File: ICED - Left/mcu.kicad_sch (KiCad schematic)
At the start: 48 parts, among them P1 Conn_ARM_JTAG_SWD_10, P2 DX07S024XJ1R1100, P3 CONN_17, P4 692121130100, P5 RGB Out, Q1 TC1264, U1 MK20DX256VLH7, X1 NX3225SA-16.000MHZ-STD-CSR-

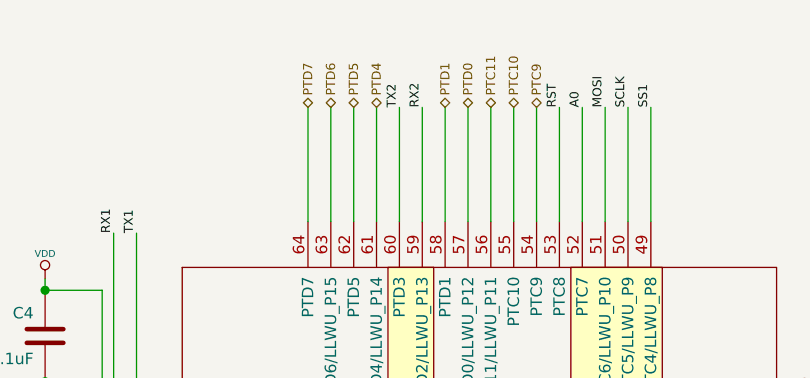
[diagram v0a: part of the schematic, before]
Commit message: mostly routed
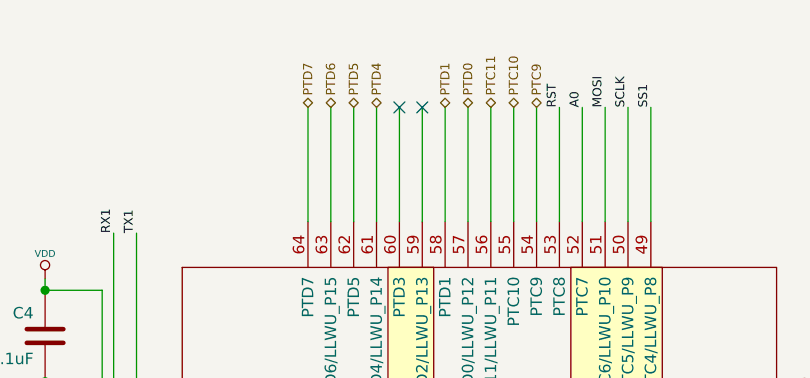
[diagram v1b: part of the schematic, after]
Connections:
- net RX2: no longer U1.59 (PTD2/LLWU_P13)
- net TX2: no longer U1.60 (PTD3)
- no-connect marks 16 -> 18
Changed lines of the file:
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@@
   (no_connect (at 134.62 111.76))
   (no_connect (at 137.16 111.76))
+  (no_connect (at 139.7 22.86))
+  (no_connect (at 142.24 22.86))
   (no_connect (at 228.6 85.09))
   (wire (pts (xy 16.51 63.5) (xy 16.51 64.77))
@@
     (effects (font (size 0.9906 0.9906)) (justify left bottom))
   )
-  (label "TX2" (at 139.7 22.86 90)
-    (effects (font (size 0.9906 0.9906)) (justify left bottom))
-  )
   (label "SWD_CLK" (at 139.7 146.05 270)
     (effects (font (size 0.9906 0.9906)) (justify right bottom))
   )
-  (label "RX2" (at 142.24 22.86 90)
-    (effects (font (size 0.9906 0.9906)) (justify left bottom))
-  )
   (label "RX0" (at 144.78 124.46 270)

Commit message: Second Revision Finalised
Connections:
- net INTB: no longer P3.14, P3.15, R3.1, R5.1, U1.35 (PTB0/LLWU_P5), U1.36 (PTB1)
- new net SCL0: P3.15, R3.1, U1.35 (PTB0/LLWU_P5)
- new net SDA0: P3.14, R5.1, U1.36 (PTB1)
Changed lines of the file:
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@@
   (junction (at 238.76 85.09) (diameter 1.016) (color 0 0 0 0))
   (junction (at 240.03 135.89) (diameter 1.016) (color 0 0 0 0))
-  (junction (at 240.03 148.59) (diameter 1.016) (color 0 0 0 0))
   (junction (at 240.03 153.67) (diameter 1.016) (color 0 0 0 0))
   (junction (at 242.57 46.99) (diameter 1.016) (color 0 0 0 0))
   (junction (at 245.11 135.89) (diameter 1.016) (color 0 0 0 0))
-  (junction (at 245.11 148.59) (diameter 1.016) (color 0 0 0 0))
   (junction (at 245.11 151.13) (diameter 1.016) (color 0 0 0 0))
   (junction (at 245.11 156.21) (diameter 1.016) (color 0 0 0 0))
@@
     (stroke (width 0) (type solid) (color 0 0 0 0))
   )
-  (wire (pts (xy 233.68 148.59) (xy 240.03 148.59))
+  (wire (pts (xy 233.68 148.59) (xy 250.19 148.59))
     (stroke (width 0) (type solid) (color 0 0 0 0))
   )
@@
     (stroke (width 0) (type solid) (color 0 0 0 0))
   )
-  (wire (pts (xy 240.03 148.59) (xy 245.11 148.59))
-    (stroke (width 0) (type solid) (color 0 0 0 0))
-  )
   (wire (pts (xy 240.03 153.67) (xy 251.46 153.67))
     (stroke (width 0) (type solid) (color 0 0 0 0))
@@
     (stroke (width 0) (type solid) (color 0 0 0 0))
   )
-  (wire (pts (xy 245.11 148.59) (xy 250.19 148.59))
-    (stroke (width 0) (type solid) (color 0 0 0 0))
-  )
